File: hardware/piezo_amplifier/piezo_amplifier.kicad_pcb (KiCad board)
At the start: 2 copper layers, 72 x 32 mm, 14 parts, among them J1 piezo1, J2 Conn_01x04, U1 LM358

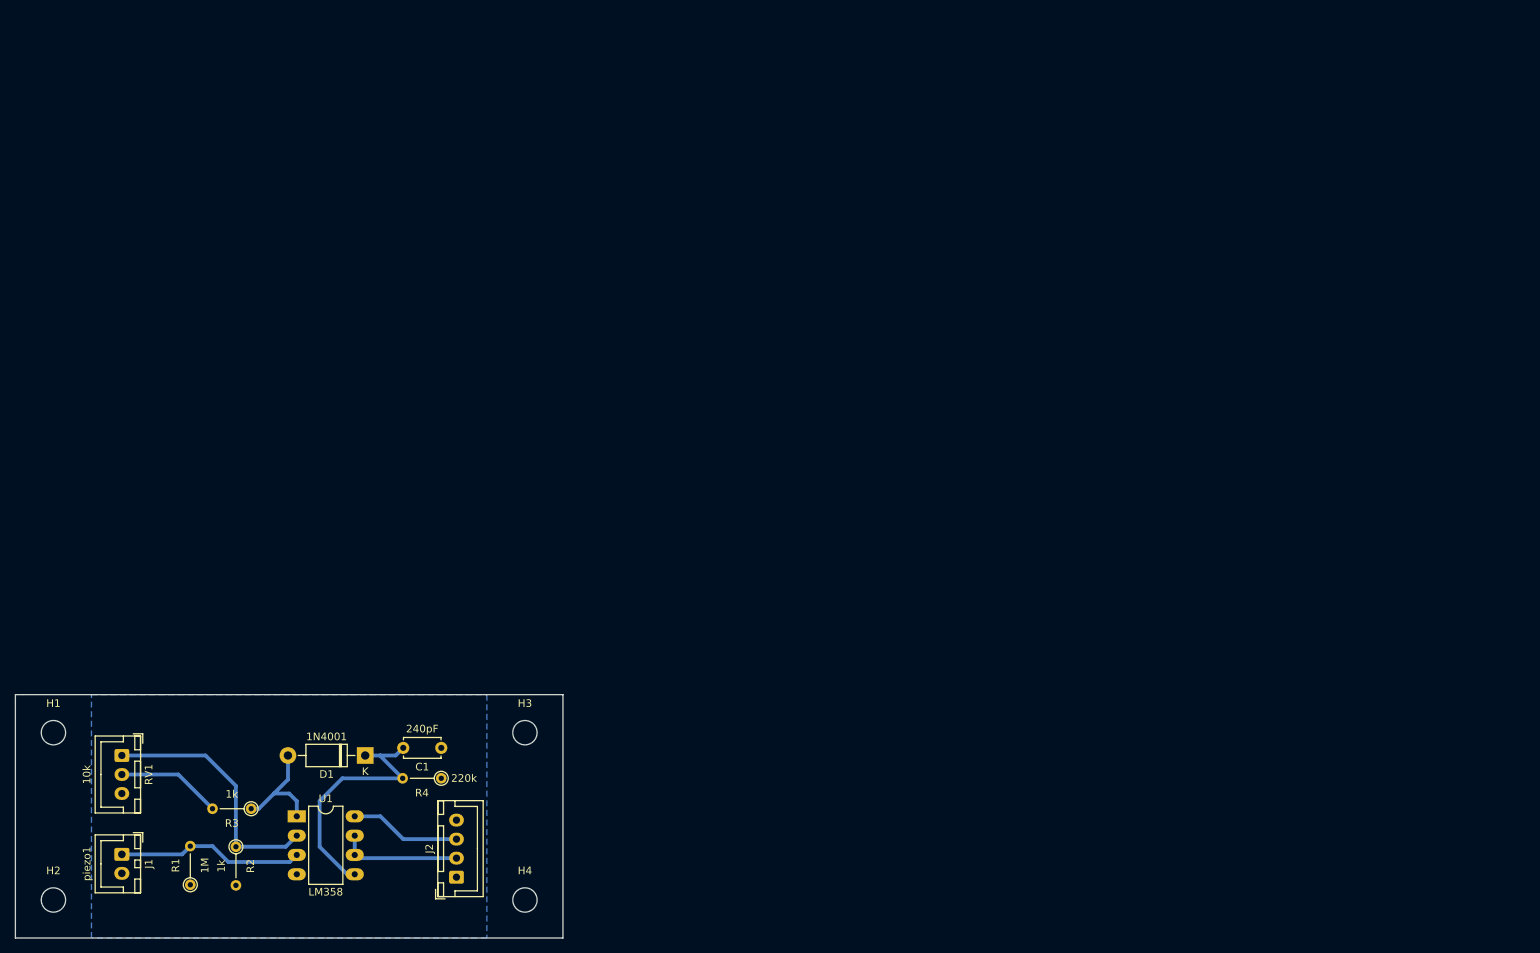
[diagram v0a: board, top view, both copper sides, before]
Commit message: update piezo amplfier
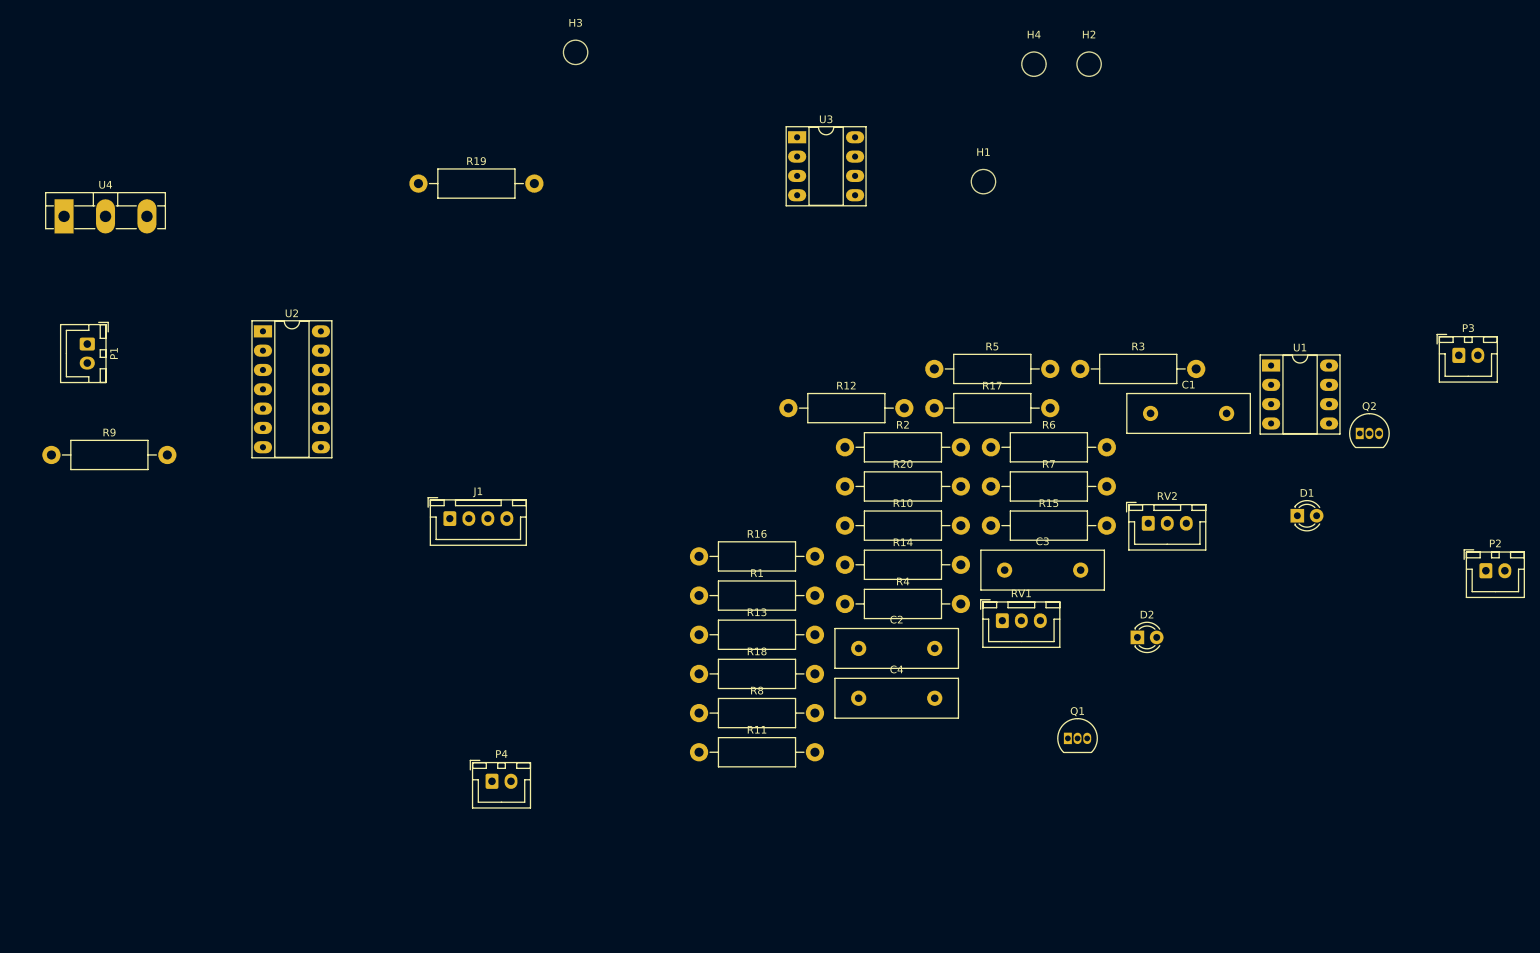
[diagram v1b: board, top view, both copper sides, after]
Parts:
- removed J2: Conn_01x04, Connector_JST:JST_XH_B4B-XH-A_1x04_P2.50mm_Vertical
- added C2: 22pF, Capacitor_THT:C_Disc_D16.0mm_W5.0mm_P10.00mm, F.Cu at (176.9, 95.9)
- added C3: 22pF, Capacitor_THT:C_Disc_D16.0mm_W5.0mm_P10.00mm, F.Cu at (196.1, 85.6)
- added C4: 22pF, Capacitor_THT:C_Disc_D16.0mm_W5.0mm_P10.00mm, F.Cu at (176.9, 102.5)
- added D2: LED, LED_THT:LED_D3.0mm_Clear, F.Cu at (213.5, 94.5)
- added P1: piezzo1, Connector_JST:JST_XH_B2B-XH-A_1x02_P2.50mm_Vertical, F.Cu at (75.5, 55.9)
- added P2: 12V, Connector_JST:JST_XH_B2B-XH-A_1x02_P2.50mm_Vertical, F.Cu at (259.4, 85.7)
- added P3: 12V, Connector_JST:JST_XH_B2B-XH-A_1x02_P2.50mm_Vertical, F.Cu at (255.8, 57.4)
- added P4: piezzo2, Connector_JST:JST_XH_B2B-XH-A_1x02_P2.50mm_Vertical, F.Cu at (128.7, 113.4)
- added Q1: PN2222A, Package_TO_SOT_THT:TO-92_Inline, F.Cu at (204.4, 107.8)
- added Q2: PN2222A, Package_TO_SOT_THT:TO-92_Inline, F.Cu at (242.8, 67.7)
- added R10: 270, Resistor_THT:R_Axial_DIN0411_L9.9mm_D3.6mm_P15.24mm_Horizontal, F.Cu at (175.1, 79.8)
- added R11: 100M, Resistor_THT:R_Axial_DIN0411_L9.9mm_D3.6mm_P15.24mm_Horizontal, F.Cu at (155.9, 109.6)
- added R12: 10k, Resistor_THT:R_Axial_DIN0411_L9.9mm_D3.6mm_P15.24mm_Horizontal, F.Cu at (167.6, 64.3)
- added R13: 20k, Resistor_THT:R_Axial_DIN0411_L9.9mm_D3.6mm_P15.24mm_Horizontal, F.Cu at (155.9, 94.1)
- added R14: 10k, Resistor_THT:R_Axial_DIN0411_L9.9mm_D3.6mm_P15.24mm_Horizontal, F.Cu at (175.1, 84.9)
- added R15: 3k, Resistor_THT:R_Axial_DIN0411_L9.9mm_D3.6mm_P15.24mm_Horizontal, F.Cu at (194.3, 79.8)
- added R16: 10k, Resistor_THT:R_Axial_DIN0411_L9.9mm_D3.6mm_P15.24mm_Horizontal, F.Cu at (155.9, 83.8)
- added R17: 3k, Resistor_THT:R_Axial_DIN0411_L9.9mm_D3.6mm_P15.24mm_Horizontal, F.Cu at (186.8, 64.3)
- added R18: 270, Resistor_THT:R_Axial_DIN0411_L9.9mm_D3.6mm_P15.24mm_Horizontal, F.Cu at (155.9, 99.3)
- added R19: 100M, Resistor_THT:R_Axial_DIN0411_L9.9mm_D3.6mm_P15.24mm_Horizontal, F.Cu at (119.0, 34.8)
- added R20: 270, Resistor_THT:R_Axial_DIN0411_L9.9mm_D3.6mm_P15.24mm_Horizontal, F.Cu at (175.1, 74.6)
- added R5: 3k, Resistor_THT:R_Axial_DIN0411_L9.9mm_D3.6mm_P15.24mm_Horizontal, F.Cu at (186.8, 59.2)
- added R6: 10k, Resistor_THT:R_Axial_DIN0411_L9.9mm_D3.6mm_P15.24mm_Horizontal, F.Cu at (194.3, 69.5)
- added R7: 3k, Resistor_THT:R_Axial_DIN0411_L9.9mm_D3.6mm_P15.24mm_Horizontal, F.Cu at (194.3, 74.6)
- added R8: 270, Resistor_THT:R_Axial_DIN0411_L9.9mm_D3.6mm_P15.24mm_Horizontal, F.Cu at (155.9, 104.4)
- added R9: 100M, Resistor_THT:R_Axial_DIN0411_L9.9mm_D3.6mm_P15.24mm_Horizontal, F.Cu at (70.7, 70.5)
- added RV2: R_Potentiometer, Connector_JST:JST_XH_B3B-XH-A_1x03_P2.50mm_Vertical, F.Cu at (215.0, 79.5)
- added U2: Opamp_Quad, Package_DIP:DIP-14_W7.62mm_Socket_LongPads, F.Cu at (98.6, 54.2)
- added U3: LM393, Package_DIP:DIP-8_W7.62mm_Socket_LongPads, F.Cu at (168.8, 28.7)
- added U4: L7806, Package_TO_SOT_THT:TO-3P-3_Vertical, F.Cu at (72.4, 39.1)
- C1: value 240pF -> 22pF; footprint Capacitor_THT:C_Disc_D4.7mm_W2.5mm_P5.00mm -> Capacitor_THT:C_Disc_D16.0mm_W5.0mm_P10.00mm
- D1: value 1N4001 -> LED; footprint Diode_THT:D_DO-41_SOD81_P10.16mm_Horizontal -> LED_THT:LED_D3.0mm_Clear
- J1: value piezo1 -> Conn_01x04_Female; footprint Connector_JST:JST_XH_B2B-XH-A_1x02_P2.50mm_Vertical -> Connector_JST:JST_XH_B4B-XH-A_1x04_P2.50mm_Vertical
- R1: value 1M -> 100M; footprint Resistor_THT:R_Axial_DIN0204_L3.6mm_D1.6mm_P5.08mm_Vertical -> Resistor_THT:R_Axial_DIN0411_L9.9mm_D3.6mm_P15.24mm_Horizontal
- R2: value 1k -> 10k; footprint Resistor_THT:R_Axial_DIN0204_L3.6mm_D1.6mm_P5.08mm_Vertical -> Resistor_THT:R_Axial_DIN0411_L9.9mm_D3.6mm_P15.24mm_Horizontal
- R3: value 1k -> 20k; footprint Resistor_THT:R_Axial_DIN0204_L3.6mm_D1.6mm_P5.08mm_Vertical -> Resistor_THT:R_Axial_DIN0411_L9.9mm_D3.6mm_P15.24mm_Horizontal
- R4: value 220k -> 10k; footprint Resistor_THT:R_Axial_DIN0204_L3.6mm_D1.6mm_P5.08mm_Vertical -> Resistor_THT:R_Axial_DIN0411_L9.9mm_D3.6mm_P15.24mm_Horizontal
- RV1: value 10k -> R_Potentiometer
- U1: value LM358 -> LM393; footprint Package_DIP:DIP-8_W7.62mm_LongPads -> Package_DIP:DIP-8_W7.62mm_Socket_LongPads
- moved H2 175.0 mm to (207.2, 19.1)
- moved H1 142.1 mm to (193.3, 34.5)
- moved U1 141.2 mm to (231.1, 58.7)
- moved H4 128.7 mm to (199.9, 19.1)
- moved D1 126.6 mm to (234.6, 78.5), turned to 0 degrees
- moved R3 123.4 mm to (206.0, 59.2), turned to 0 degrees
- moved RV1 117.1 mm to (195.8, 92.3), turned to 0 degrees
- moved C1 103.1 mm to (215.3, 65.0), turned to 0 degrees
- moved R2 95.8 mm to (175.1, 69.5), turned to 0 degrees
- moved H3 89.7 mm to (139.7, 17.5)
- moved R1 76.9 mm to (155.9, 89.0), turned to 0 degrees
- moved J1 61.7 mm to (123.1, 78.8), turned to 0 degrees
- moved R4 57.8 mm to (175.1, 90.1), turned to 0 degrees
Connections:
- C1 pad 1: GND -> Net-(C1-Pad1)
- D1 pad 1: Net-(C1-Pad2) -> Net-(D1-Pad1)
- J1 pad 2: GND -> Net-(J1-Pad2)
- R1 pad 1: GND -> Net-(C1-Pad1)
- R1 pad 2: Net-(J1-Pad1) -> Net-(C1-Pad2)
- R2 pad 1: Net-(R2-Pad1) -> Net-(P1-Pad1)
- R2 pad 2: GND -> Net-(C1-Pad1)
- R3 pad 1: Net-(D1-Pad2) -> Net-(R3-Pad1)
- R4 pad 1: GND -> Net-(P1-Pad2)
- R4 pad 2: Net-(C1-Pad2) -> Net-(C2-Pad1)
- RV1 pad 1: Net-(R2-Pad1) -> +12V
- RV1 pad 2: Net-(R3-Pad2) -> Net-(RV1-Pad2)
- RV1 pad 3: Net-(RV1-Pad3) -> GND
- U1 pad 1: Net-(D1-Pad2) -> (no net)
- U1 pad 2: Net-(R2-Pad1) -> (no net)
- U1 pad 3: Net-(J1-Pad1) -> (no net)
- U1 pad 5: Net-(C1-Pad2) -> (no net)
- U1 pad 6: Net-(J2-Pad2) -> (no net)
- U1 pad 7: Net-(J2-Pad2) -> (no net)
- U1 pad 8: +5V -> +12V
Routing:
- net Net-(C1-Pad2): track 33.9 -> 0.00 mm
- net Net-(R2-Pad1): track 33.3 -> 0.00 mm
- net Net-(J1-Pad1): track 24.7 -> 0.00 mm
- net Net-(J2-Pad2): track 16.1 -> 0.00 mm
- net Net-(D1-Pad2): track 15.0 -> 0.00 mm
- net +5V: track 14.6 -> 0.00 mm
- net Net-(R3-Pad2): track 13.8 -> 0.00 mm
- removed copper zone on B.Cu, net GND
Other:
- board outline removed
- net class Default removed
